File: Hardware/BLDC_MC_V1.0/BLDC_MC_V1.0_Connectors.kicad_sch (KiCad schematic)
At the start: 1 part, among them J6 Screw_Terminal_01x02

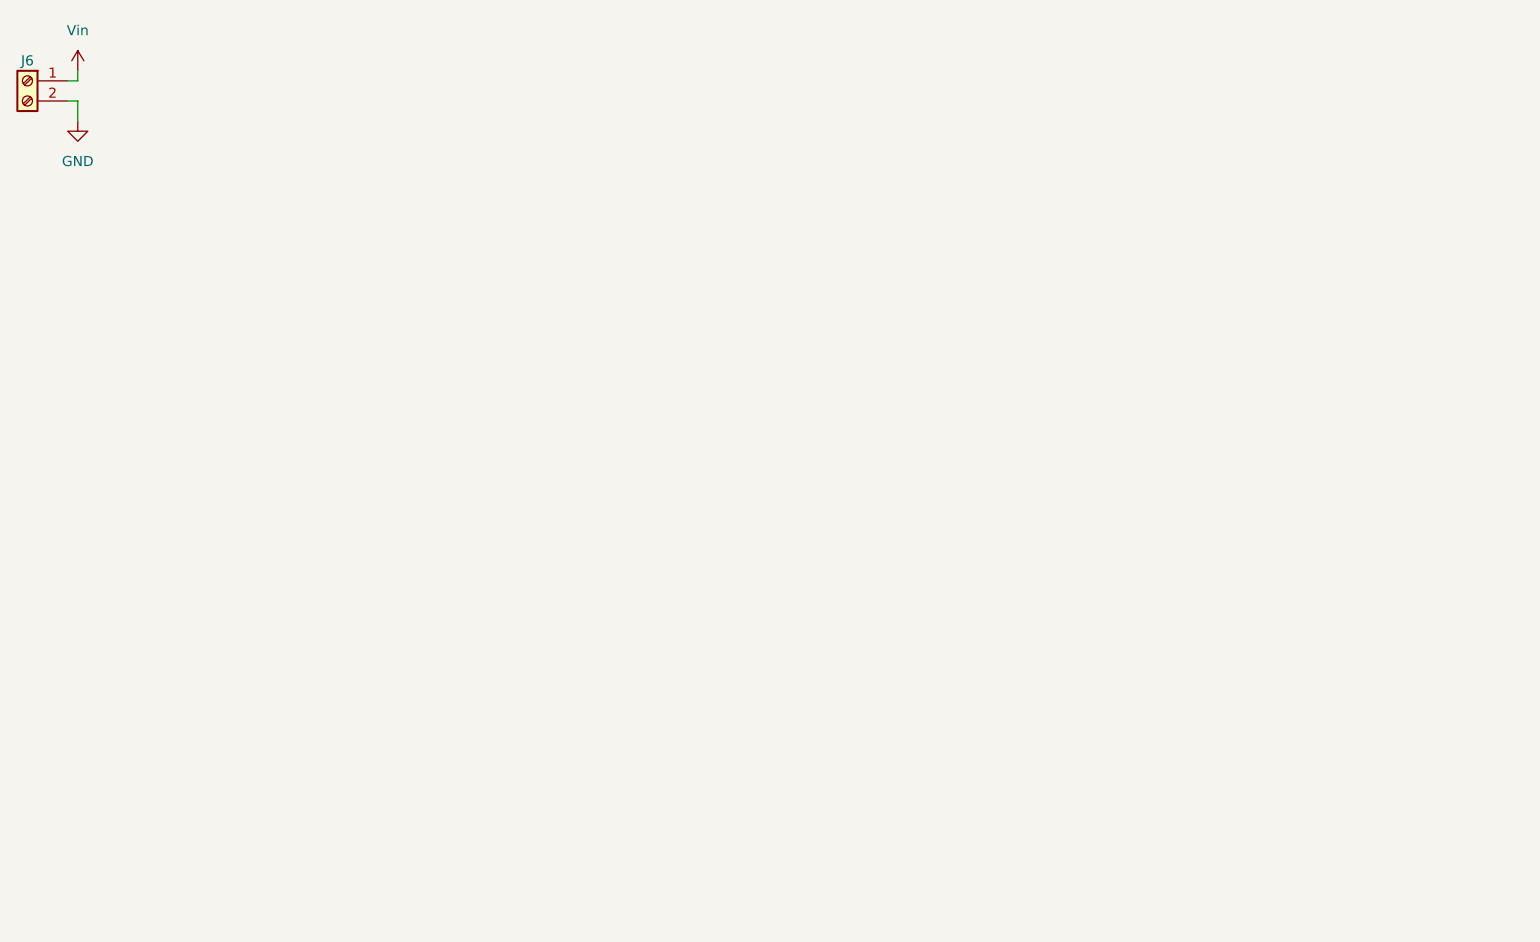
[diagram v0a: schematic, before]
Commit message: Add the connectors used in the project ( power, sensor and communication connectors)
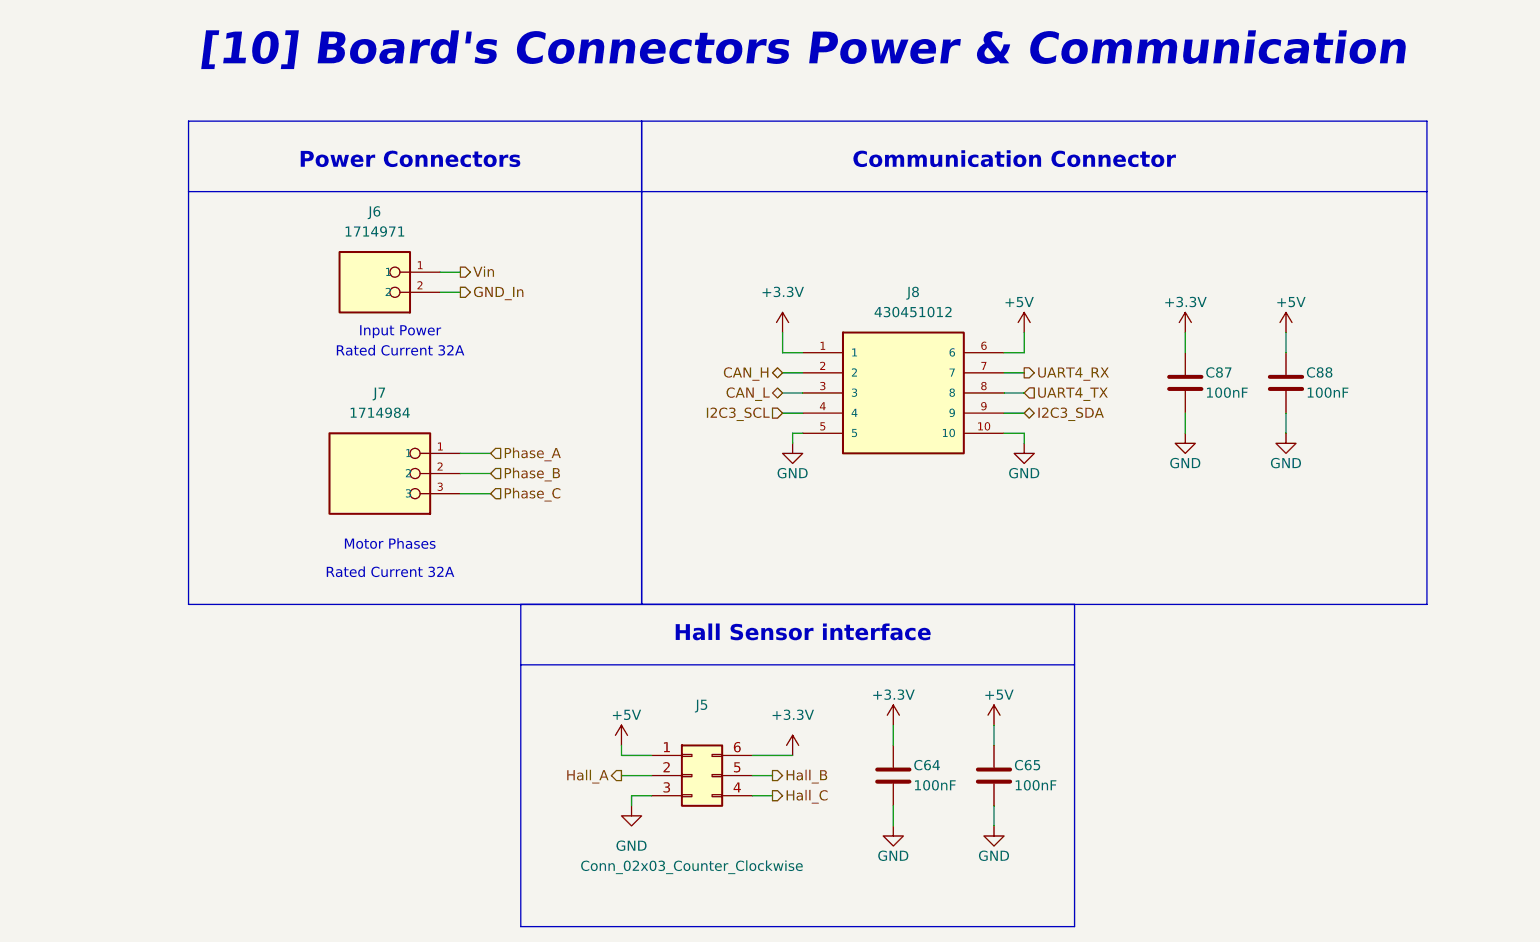
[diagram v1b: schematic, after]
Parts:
- removed J6: Screw_Terminal_01x02, TerminalBlock_Phoenix:TerminalBlock_Phoenix_MKDS-1,5-2-5.08_1x02_P5.08mm_Horizontal, symbol Connector:Screw_Terminal_01x02
- added C64, C65, C87, C88: 100nF, Capacitor_SMD:C_0805_2012Metric, symbol Device:C
- added J5: Conn_02x03_Counter_Clockwise, Connector_Molex:Molex_Micro-Fit_3.0_43045-0612_2x03_P3.00mm_Vertical, symbol Connector_Generic:Conn_02x03_Counter_Clockwise
- added J6: 1714971, BLDC_Motor_Driver_Components_Footprint:PHOENIX_1714971, symbol 1714971:1714971
- added J7: 1714984, BLDC_Motor_Driver_Components_Footprint:PHOENIX_1714984, symbol 1714984:1714984
- added J8: 430451012, BLDC_Motor_Driver_Components_Footprint:MOLEX_430451012, symbol 430451012:430451012
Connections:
- net GND: now also C64.2, C65.2, C87.2, C88.2, J5.3 (Pin_3), J8.10, J8.5
- net Vin: now also J6.1
- new net +3.3V: C64.1, C87.1, J5.6 (Pin_6), J8.1
- new net +5V: C65.1, C88.1, J5.1 (Pin_1), J8.6
- new net CAN_H: J8.2
- new net CAN_L: J8.3
- new net GND_In: J6.2
- new net Hall_A: J5.2 (Pin_2)
- new net Hall_B: J5.5 (Pin_5)
- new net Hall_C: J5.4 (Pin_4)
- new net I2C3_SCL: J8.4
- new net I2C3_SDA: J8.9
- new net Phase_A: J7.1
- new net Phase_B: J7.2
- new net Phase_C: J7.3
- new net UART4_RX: J8.7
- new net UART4_TX: J8.8
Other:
- note added: "Communication Connector"
- note added: "Hall Sensor interface"
- note added: "Input Power"
- note added: "Motor Phases"
- note added: "Power Connectors"
- note added: "Rated Current 32A"
- note added: "[10] Board's Connectors Power & Communication"

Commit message: Add TVS protection for communication connector
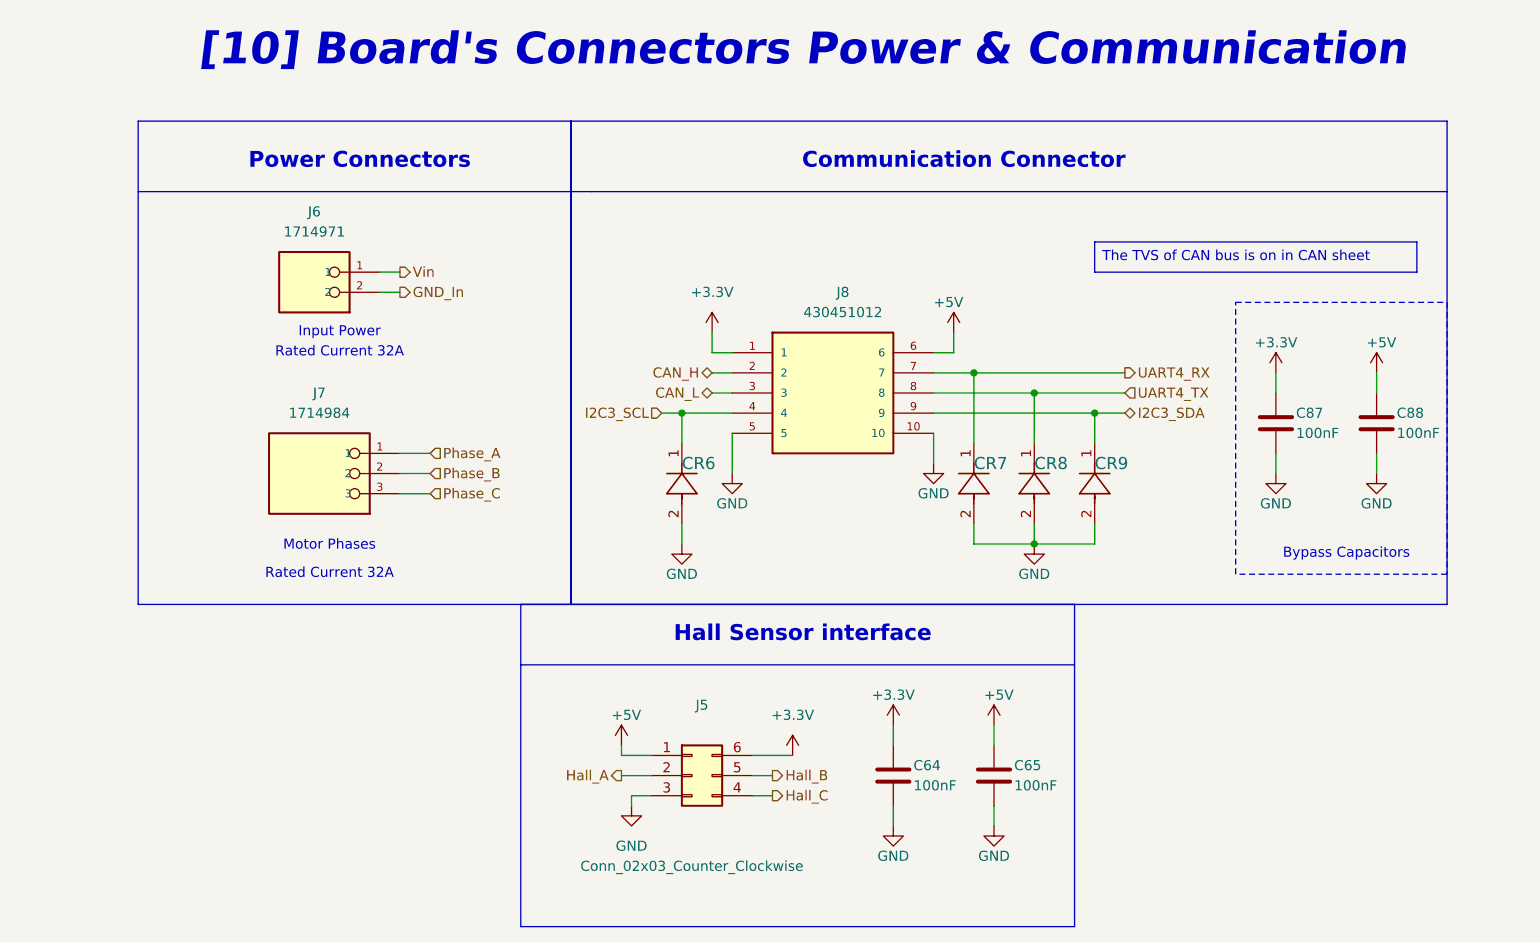
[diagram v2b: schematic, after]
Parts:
- added CR6, CR7, CR8, CR9: PESD3V3L1BA_115, BLDC_Motor_Driver_Components_Footprint:DIODE_PESD3V3L1BA_115_NEX, symbol PESD3V3L1BA,115:PESD3V3L1BA_115
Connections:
- net GND: now also CR6.2, CR7.2, CR8.2, CR9.2
- net I2C3_SCL: now also CR6.1
- net I2C3_SDA: now also CR9.1
- net UART4_RX: now also CR7.1
- net UART4_TX: now also CR8.1
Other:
- note added: "Bypass Capacitors"
- moved on the sheet: C87, C88, J6, J7, J8

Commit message: Solve all errors and wornings in project
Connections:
- net Vin renamed Vin_DC
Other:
- title: BLDC_MC_V1.0_Connectors -> ${Project_Name}
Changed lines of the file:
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@@
 	(paper "A4")
 	(title_block
-		(title "BLDC_MC_V1.0_Connectors")
+		(title "${Project_Name}")
 		(date "2026-03-08")
 		(rev "V1")
@@
 		)
 	)
-	(hierarchical_label "Vin"
+	(hierarchical_label "Vin_DC"
 		(shape output)
 		(at 96.52 68.58 0)
@@
 			)
 		)
-		(property "Datasheet" "https://www.lcsc.com/datasheet/C28233.pdf"
+		(property "Datasheet" "~"
 			(at 158.75 132.08 0)
 			(effects
@@
 			)
 		)
-		(property "Datasheet" "https://www.lcsc.com/datasheet/C28233.pdf"
+		(property "Datasheet" "~"
 			(at 171.45 132.08 0)
 			(effects
@@
 			)
 		)
-		(property "Datasheet" "https://www.lcsc.com/datasheet/C28233.pdf"
+		(property "Datasheet" "~"
 			(at 207.01 87.63 0)
 			(effects
@@
 			)
 		)
-		(property "Datasheet" "https://www.lcsc.com/datasheet/C28233.pdf"
+		(property "Datasheet" "~"
 			(at 219.71 87.63 0)
 			(effects

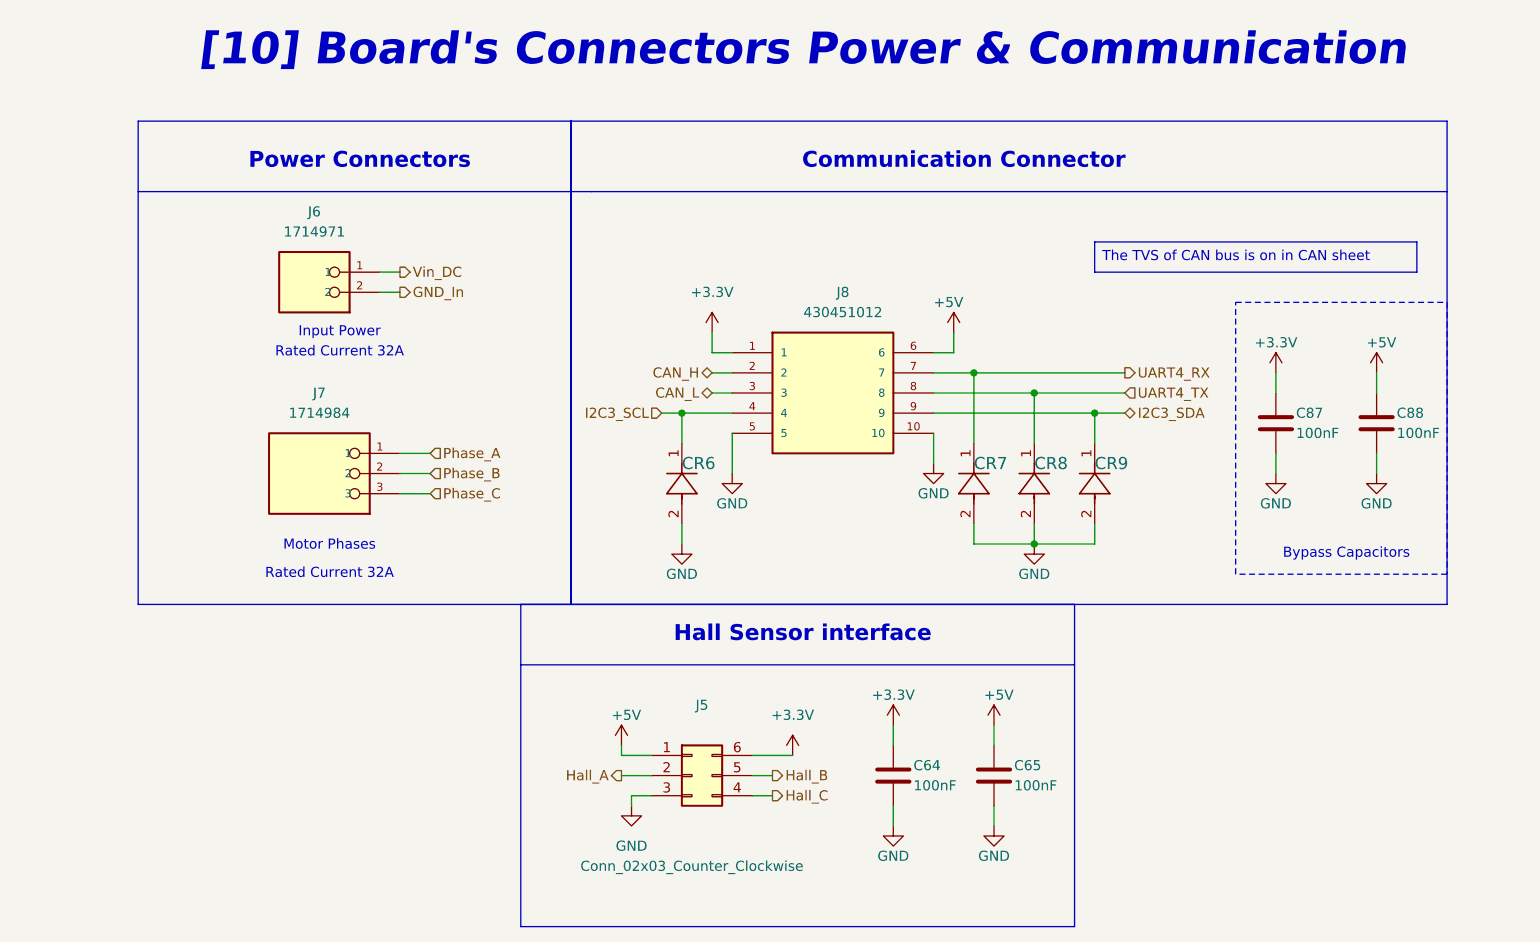
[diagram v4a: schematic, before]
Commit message: Update the component placement of the board
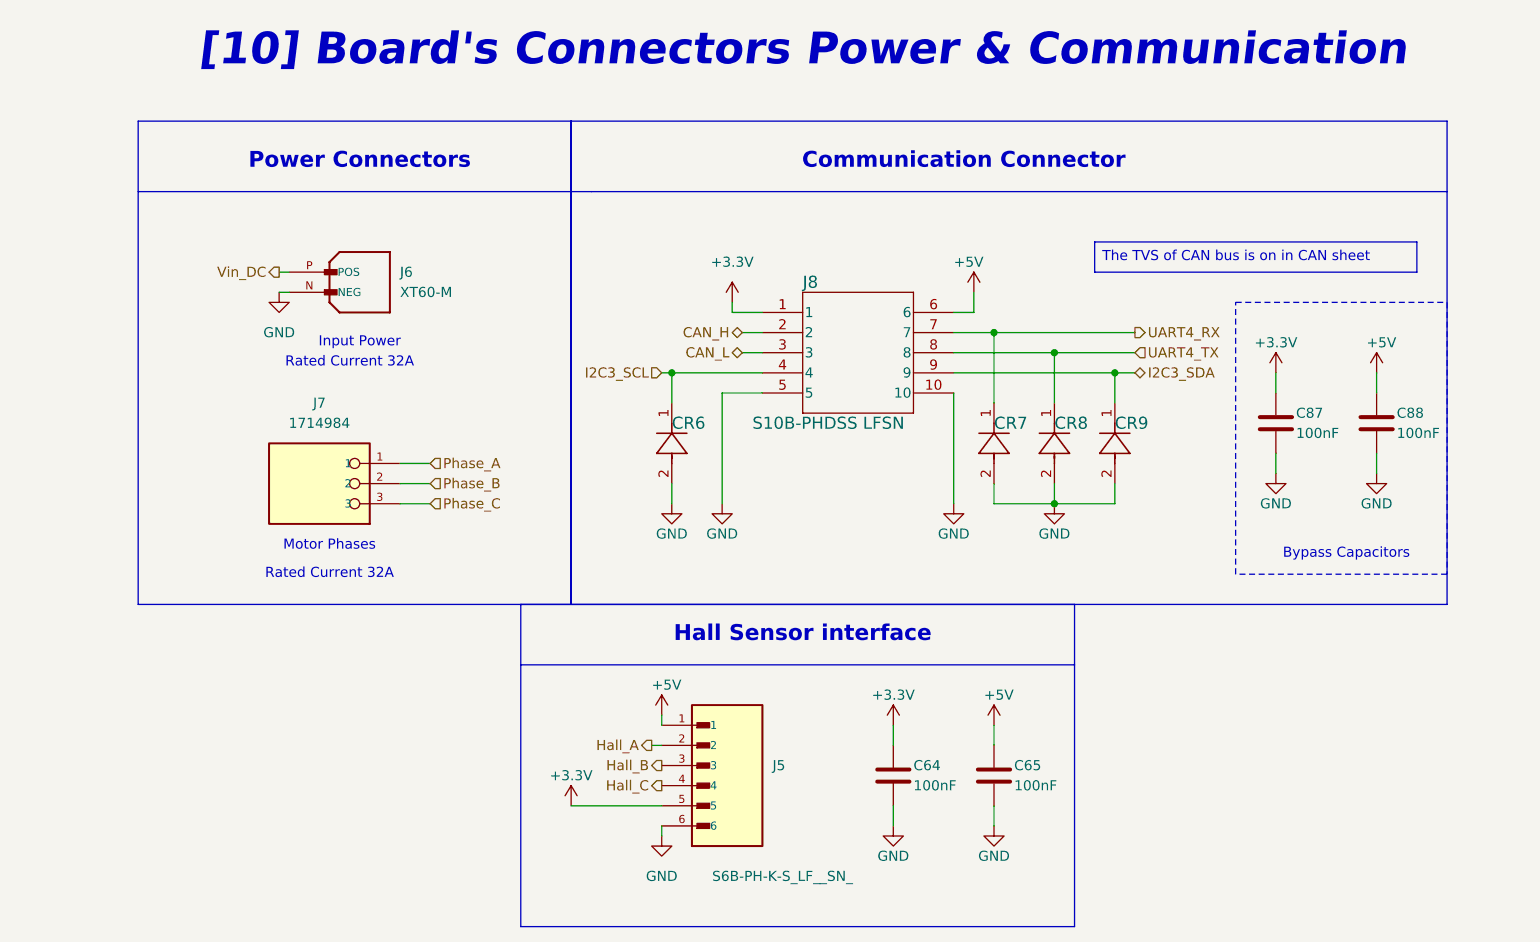
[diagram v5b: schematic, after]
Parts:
- removed J5: Conn_02x03_Counter_Clockwise, Connector_Molex:Molex_Micro-Fit_3.0_43045-0612_2x03_P3.00mm_Vertical, symbol Connector_Generic:Conn_02x03_Counter_Clockwise
- removed J6: 1714971, BLDC_Motor_Driver_Components_Footprint:PHOENIX_1714971, symbol 1714971:1714971
- removed J8: 430451012, BLDC_Motor_Driver_Components_Footprint:MOLEX_430451012, symbol 430451012:430451012
- added J5: S6B-PH-K-S_LF__SN_, BLDC_Motor_Driver_Components_Footprint:JST_S6B-PH-K-S_LF__SN_, symbol S6B-PH-K-S_LF__SN_:S6B-PH-K-S_LF__SN_
- added J6: XT60-M, BLDC_Motor_Driver_Components_Footprint:AMASS_XT60-M, symbol XT60-M:XT60-M
- added J8: S10B-PHDSS LFSN, BLDC_Motor_Driver_Components_Footprint:CONN_S10B-PHDSS_JST, symbol S10B-PHDSS(LF)(SN):S10B-PHDSS_LFSN
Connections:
- net +3.3V: now also J5.5, J8.1
- net +5V: now also J5.1, J8.6
- net CAN_H: now also J8.2
- net CAN_L: now also J8.3
- net GND: now also J5.6, J6.N (NEG), J8.10, J8.5
- net Hall_A: now also J5.2
- net Hall_B: now also J5.3
- net Hall_C: now also J5.4
- net I2C3_SCL: now also J8.4
- net I2C3_SDA: now also J8.9
- net UART4_RX: now also J8.7
- net UART4_TX: now also J8.8
- net Vin_DC: now also J6.P (POS)
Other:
- moved on the sheet: CR6, CR7, CR8, CR9, J7

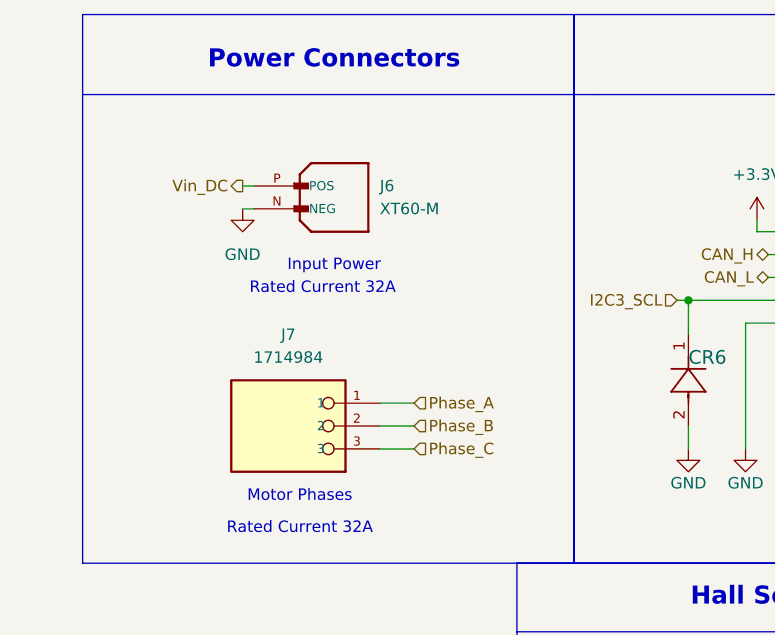
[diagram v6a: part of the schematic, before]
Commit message: Routing Power plans and change the power connedtors
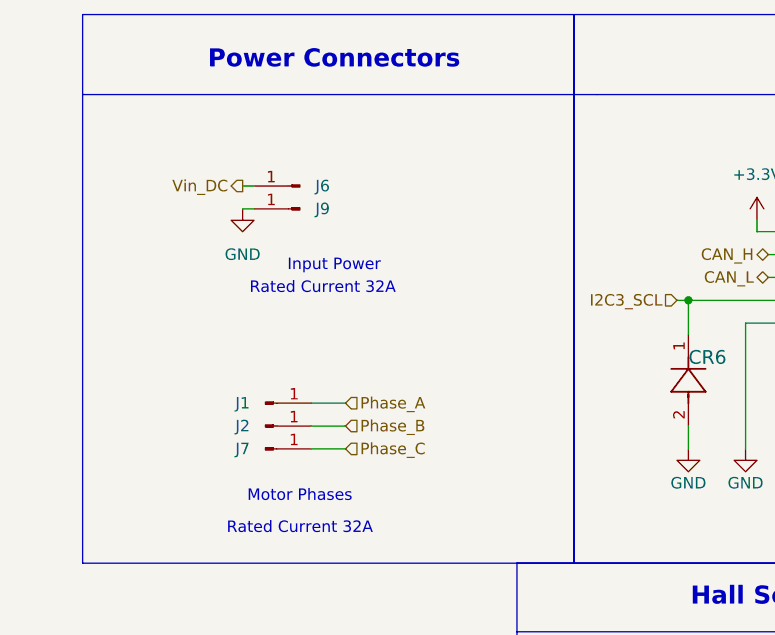
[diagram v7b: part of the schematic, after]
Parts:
- removed J6: XT60-M, BLDC_Motor_Driver_Components_Footprint:AMASS_XT60-M, symbol XT60-M:XT60-M
- removed J7: 1714984, BLDC_Motor_Driver_Components_Footprint:PHOENIX_1714984, symbol 1714984:1714984
- added J1, J2, J6, J7, J9: Conn_01x01_Pin, BLDC_Motor_Driver_Components_Footprint:PWR_CON_L, symbol Connector:Conn_01x01_Pin
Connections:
- net GND: now also J9.1 (Pin_1)
- net Phase_A: now also J1.1 (Pin_1)
- net Phase_B: now also J2.1 (Pin_1)
- net Phase_C: now also J7.1 (Pin_1)
- net Vin_DC: now also J6.1 (Pin_1)
